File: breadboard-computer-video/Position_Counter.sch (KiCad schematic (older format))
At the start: 11 parts

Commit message: added things
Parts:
- removed U?: 74LS20, symbol 74xx:74LS20
- added U?: 74LS08, symbol 74xx:74LS08
- added U?: 74LS04, symbol 74xx:74LS04
- added U?: 74LS32, symbol 74xx:74LS32
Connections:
- wire segments 207 -> 209
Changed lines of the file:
@@
 Connection ~ 5650 2600
 Wire Wire Line
-	6650 2600 6650 5750
+	6650 2600 6650 3850
 Connection ~ 6650 2600
 Wire Wire Line
 	6650 2600 5650 2600
-Connection ~ 6650 5750
-Wire Wire Line
-	6650 5750 6950 5750
 NoConn ~ 3650 6200
 NoConn ~ 3450 6200
@@
 NoConn ~ 5350 6200
 Wire Wire Line
-	5550 6200 5550 6050
+	5550 6200 5550 6100
 Wire Wire Line
-	5550 6050 6100 6050
+	5550 6100 6100 6100
 Wire Wire Line
-	5250 6200 5250 5950
+	5250 6200 5250 6000
 Wire Wire Line
-	5250 5950 6100 5950
+	5250 6000 6100 6000
 Wire Wire Line
-	6700 6100 6800 6100
-Wire Wire Line
-	6800 6100 6800 7350
+	6700 6100 6750 6100
 Wire Wire Line
 	6800 7350 6250 7350
@@
 	1    0    0    -1
 $EndComp
-Wire Wire Line
-	4850 5750 6650 5750
 Connection ~ 4850 5750
 $Comp
-L 74xx:74LS20 U?
-U 2 1 5DE95783
+L 74xx:74LS08 U?
+U 1 1 5DED443E
 P 6400 6100
-F 0 "U?" H 6400 6475 50  0000 C CNN
-F 1 "74LS20" H 6400 6384 50  0000 C CNN
+F 0 "U?" H 6400 6425 50  0000 C CNN
+F 1 "74LS08" H 6400 6334 50  0000 C CNN
 F 2 "" H 6400 6100 50  0001 C CNN
-F 3 "http://www.ti.com/lit/gpn/sn74LS20" H 6400 6100 50  0001 C CNN
-	2    6400 6100
+F 3 "http://www.ti.com/lit/gpn/sn74LS08" H 6400 6100 50  0001 C CNN
+	1    6400 6100
 	1    0    0    -1
 $EndComp
 Wire Wire Line
-	6100 6150 6100 6250
+	6100 6100 6100 6200
+$Comp
+L 74xx:74LS04 U?
+U 1 1 5DF0C5CD
+P 6800 6400
+F 0 "U?" V 6754 6580 50  0000 L CNN
+F 1 "74LS04" V 6845 6580 50  0000 L CNN
+F 2 "" H 6800 6400 50  0001 C CNN
+F 3 "http://www.ti.com/lit/gpn/sn74LS04" H 6800 6400 50  0001 C CNN
+	1    6800 6400
+	0    1    1    0
+$EndComp
 Wire Wire Line
-	6100 6050 6100 6150
-Connection ~ 6100 6050
-Connection ~ 6100 6150
+	6800 6700 6800 7350
+$Comp
+L 74xx:74LS32 U?
+U 1 1 5DF1C351
+P 6650 4150
+F 0 "U?" V 6696 3970 50  0000 R CNN
+F 1 "74LS32" V 6605 3970 50  0000 R CNN
+F 2 "" H 6650 4150 50  0001 C CNN
+F 3 "http://www.ti.com/lit/gpn/sn74LS32" H 6650 4150 50  0001 C CNN
+	1    6650 4150
+	0    -1   -1   0
+$EndComp
+Wire Wire Line
+	4850 5750 6550 5750
+Wire Wire Line
+	6550 4450 6550 5750
+Connection ~ 6550 5750
+Wire Wire Line
+	6550 5750 6950 5750
+Wire Wire Line
+	6750 6100 6750 4450
+Connection ~ 6750 6100
+Wire Wire Line
+	6750 6100 6800 6100
 $EndSCHEMATC

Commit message: finished
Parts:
- removed U? (x5): 74LS161, symbol 74xx:74LS161
- added U?: 74LS04, symbol 74xx:74LS04
- added U? (x6): 74LS163, symbol 74xx:74LS163
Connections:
- net labels added: A0, A1, A2, A3, A4, A5, A6, A7, A8, A9, Earth, VBLANK, VCC
- wire segments 209 -> 230
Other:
- moved on the sheet: U?A

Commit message: fixed labels
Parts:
- removed U?: 74LS161, symbol 74xx:74LS161
- gave numbers to parts that had none: 13
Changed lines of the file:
@@
 CLK
 $Comp
-L 74xx:74LS83 U?
+L 74xx:74LS83 U28
 U 1 1 5DAF14DF
 P 2550 4150
-F 0 "U?" H 2550 5131 50  0000 C CNN
+F 0 "U28" H 2550 5131 50  0000 C CNN
 F 1 "74LS83" H 2550 5040 50  0000 C CNN
 F 2 "" H 2550 4150 50  0001 C CNN
@@
 $EndComp
 $Comp
-L 74xx:74LS83 U?
+L 74xx:74LS83 U32
 U 1 1 5DAF1910
 P 5650 4150
-F 0 "U?" H 5650 5131 50  0000 C CNN
+F 0 "U32" H 5650 5131 50  0000 C CNN
 F 1 "74LS83" H 5650 5040 50  0000 C CNN
 F 2 "" H 5650 4150 50  0001 C CNN
@@
 	7750 4650 8350 4650
 $Comp
-L 74xx:74LS83 U?
+L 74xx:74LS83 U37
 U 1 1 5DC079C4
 P 8850 4150
-F 0 "U?" H 8850 5131 50  0000 C CNN
+F 0 "U37" H 8850 5131 50  0000 C CNN
 F 1 "74LS83" H 8850 5040 50  0000 C CNN
 F 2 "" H 8850 4150 50  0001 C CNN
@@
 	6250 7250 6250 7100
 $Comp
-L 74xx:74LS20 U?
+L 74xx:74LS20 U30
 U 1 1 5DE7A035
 P 3750 5650
-F 0 "U?" H 3750 6025 50  0000 C CNN
+F 0 "U30" H 3750 6025 50  0000 C CNN
 F 1 "74LS20" H 3750 5934 50  0000 C CNN
 F 2 "" H 3750 5650 50  0001 C CNN
@@
 Connection ~ 4850 5650
 $Comp
-L 74xx:74LS08 U?
+L 74xx:74LS08 U34
 U 1 1 5DED443E
 P 6400 6000
-F 0 "U?" H 6400 6325 50  0000 C CNN
+F 0 "U34" H 6400 6325 50  0000 C CNN
 F 1 "74LS08" H 6400 6234 50  0000 C CNN
 F 2 "" H 6400 6000 50  0001 C CNN
@@
 	6100 6000 6100 6100
 $Comp
-L 74xx:74LS04 U?
+L 74xx:74LS04 U19
 U 1 1 5DF0C5CD
 P 6800 6300
-F 0 "U?" V 6754 6480 50  0000 L CNN
+F 0 "U19" V 6754 6480 50  0000 L CNN
 F 1 "74LS04" V 6845 6480 50  0000 L CNN
 F 2 "" H 6800 6300 50  0001 C CNN
@@
 	6800 6600 6800 7250
 $Comp
-L 74xx:74LS32 U?
+L 74xx:74LS32 U35
 U 1 1 5DF1C351
 P 6650 4150
-F 0 "U?" V 6696 3970 50  0000 R CNN
+F 0 "U35" V 6696 3970 50  0000 R CNN
 F 1 "74LS32" V 6605 3970 50  0000 R CNN
 F 2 "" H 6650 4150 50  0001 C CNN
@@
 	6150 2500 9350 2500
 $Comp
-L 74xx:74LS04 U?
+L 74xx:74LS04 U19
 U 2 1 5E085A92
 P 1250 1700
-F 0 "U?" V 1204 1880 50  0000 L CNN
+F 0 "U19" V 1204 1880 50  0000 L CNN
 F 1 "74LS04" V 1295 1880 50  0000 L CNN
 F 2 "" H 1250 1700 50  0001 C CNN
@@
 A9
 $Comp
-L 74xx:74LS163 U?
+L 74xx:74LS163 U27
 U 1 1 5E0C0473
 P 2550 1900
-F 0 "U?" V 2596 1056 50  0000 R CNN
+F 0 "U27" V 2596 1056 50  0000 R CNN
 F 1 "74LS163" V 2505 1056 50  0000 R CNN
 F 2 "" H 2550 1900 50  0001 C CNN
@@
 $EndComp
 $Comp
-L 74xx:74LS163 U?
+L 74xx:74LS163 U31
 U 1 1 5E0F4790
 P 5650 1900
-F 0 "U?" V 5696 1056 50  0000 R CNN
+F 0 "U31" V 5696 1056 50  0000 R CNN
 F 1 "74LS163" V 5605 1056 50  0000 R CNN
 F 2 "" H 5650 1900 50  0001 C CNN
@@
 $EndComp
 $Comp
-L 74xx:74LS163 U?
+L 74xx:74LS163 U36
 U 1 1 5E1044B1
 P 8850 1900
-F 0 "U?" V 8896 1056 50  0000 R CNN
+F 0 "U36" V 8896 1056 50  0000 R CNN
 F 1 "74LS163" V 8805 1056 50  0000 R CNN
 F 2 "" H 8850 1900 50  0001 C CNN
@@
 $EndComp
 $Comp
-L 74xx:74LS163 U?
+L 74xx:74LS163 U26
 U 1 1 5E115C5E
 P 1550 6600
-F 0 "U?" V 1596 5756 50  0000 R CNN
+F 0 "U26" V 1596 5756 50  0000 R CNN
 F 1 "74LS163" V 1505 5756 50  0000 R CNN
 F 2 "" H 1550 6600 50  0001 C CNN
@@
 $EndComp
 $Comp
-L 74xx:74LS163 U?
+L 74xx:74LS163 U29
 U 1 1 5E125B51
 P 3650 6600
-F 0 "U?" V 3696 5756 50  0000 R CNN
+F 0 "U29" V 3696 5756 50  0000 R CNN
 F 1 "74LS163" V 3605 5756 50  0000 R CNN
 F 2 "" H 3650 6600 50  0001 C CNN
@@
 $EndComp
 $Comp
-L 74xx:74LS163 U?
+L 74xx:74LS163 U33
 U 1 1 5E1357C5
 P 5750 6600
-F 0 "U?" V 5796 5756 50  0000 R CNN
+F 0 "U33" V 5796 5756 50  0000 R CNN
 F 1 "74LS163" V 5705 5756 50  0000 R CNN
 F 2 "" H 5750 6600 50  0001 C CNN
@@
 	0    -1   -1   0
 $EndComp
-$Comp
-L 74xx:74LS161 U?
-U 1 1 5DAF4BC7
-P 1550 6600
-F 0 "U?" V 1596 5756 50  0000 R CNN
-F 1 "74LS161" V 1505 5756 50  0000 R CNN
-F 2 "" H 1550 6600 50  0001 C CNN
-F 3 "http://www.ti.com/lit/gpn/sn74LS161" H 1550 6600 50  0001 C CNN
-	1    1550 6600
-	0    -1   -1   0
-$EndComp

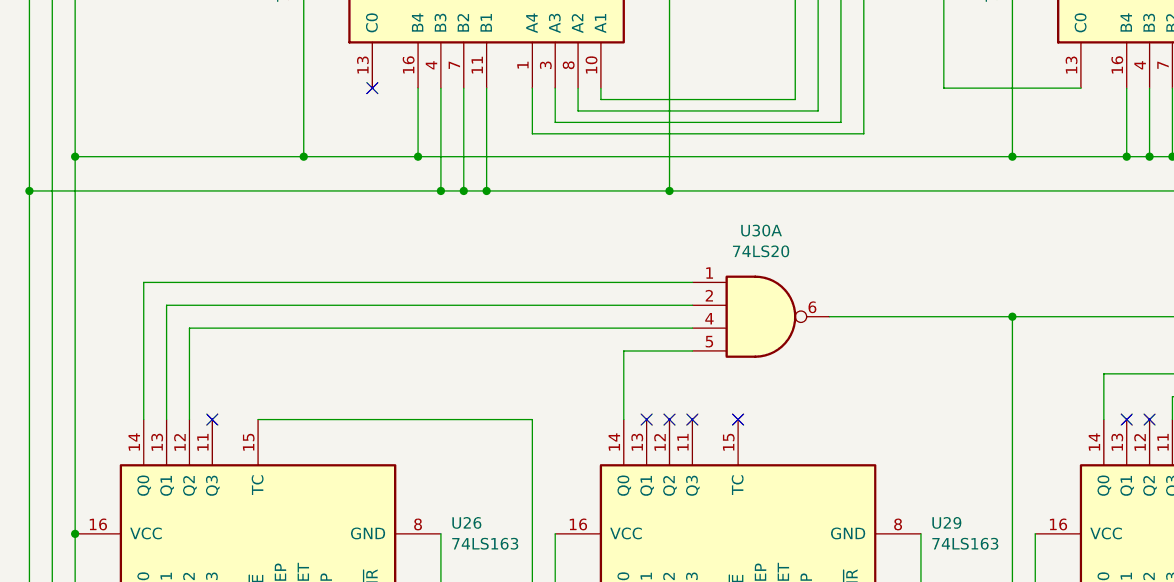
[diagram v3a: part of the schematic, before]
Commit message: Change 74LS20 to 74LS30
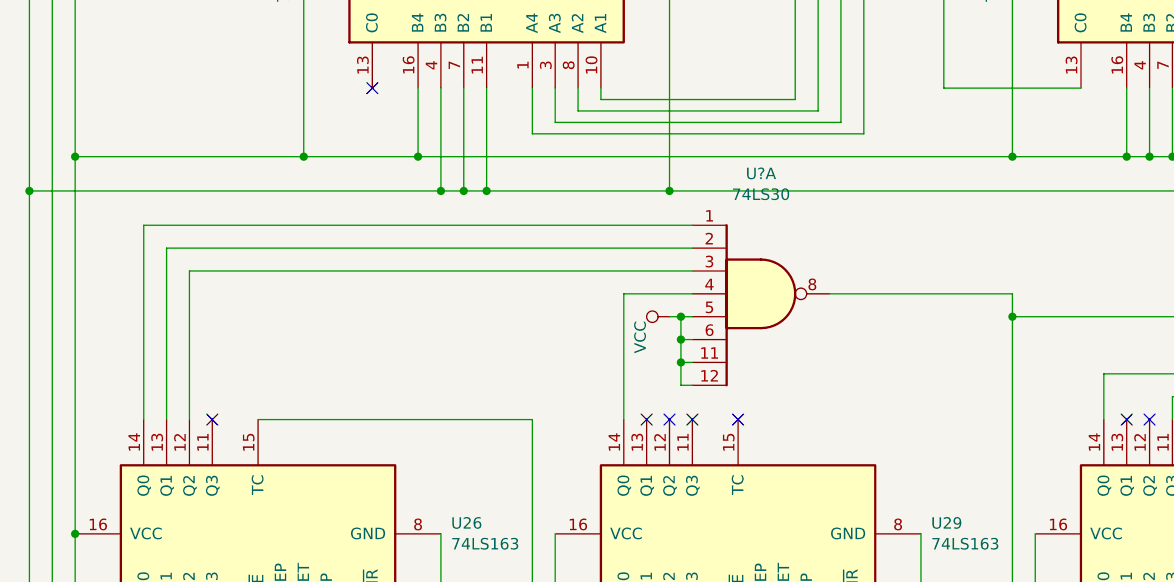
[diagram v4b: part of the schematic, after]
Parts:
- removed U30: 74LS20, symbol 74xx:74LS20
- added U?: 74LS30, symbol 74xx:74LS30
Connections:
- net VCC: now also U?.11, U?.12, U?.5, U?.6
- net at U26.14 (Q0): now also U?.1
- net at U26.13 (Q1): now also U?.2
- net at U26.12 (Q2): now also U?.3
- net at U29.14 (Q0): now also U?.4
- net at U26.1 (~MR), U29.1 (~MR), U33.2 (CP)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: now also U?.8
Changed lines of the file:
@@
 Wire Wire Line
 	2450 4650 2450 5100
-Wire Wire Line
-	2550 4650 2550 5100
 Connection ~ 2550 5100
 Wire Wire Line
@@
 	4950 7500 5750 7500
 Wire Wire Line
-	3450 5800 3150 5800
-Wire Wire Line
-	3150 5800 3150 6100
-Wire Wire Line
-	3450 5700 1250 5700
-Wire Wire Line
-	1250 5700 1250 6100
-Wire Wire Line
-	3450 5600 1150 5600
-Wire Wire Line
-	1150 5600 1150 6100
-Wire Wire Line
-	3450 5500 1050 5500
-Wire Wire Line
-	1050 5500 1050 6100
-Wire Wire Line
-	4050 5650 4850 5650
+	3450 5550 3150 5550
+Wire Wire Line
+	3150 5550 3150 6100
+Wire Wire Line
+	3450 5450 1250 5450
+Wire Wire Line
+	1250 5450 1250 6100
+Wire Wire Line
+	3450 5350 1150 5350
+Wire Wire Line
+	1150 5350 1150 6100
+Wire Wire Line
+	3450 5250 1050 5250
+Wire Wire Line
+	1050 5250 1050 6100
 Wire Wire Line
 	6050 7400 6050 7100
@@
 Wire Wire Line
 	6250 7250 6250 7100
-$Comp
-L 74xx:74LS20 U30
-U 1 1 5DE7A035
-P 3750 5650
-F 0 "U30" H 3750 6025 50  0000 C CNN
-F 1 "74LS20" H 3750 5934 50  0000 C CNN
-F 2 "" H 3750 5650 50  0001 C CNN
-F 3 "http://www.ti.com/lit/gpn/sn74LS20" H 3750 5650 50  0001 C CNN
-	1    3750 5650
-	1    0    0    -1
-$EndComp
 Connection ~ 4850 5650
 $Comp
@@
 	0    -1   -1   0
 $EndComp
+$Comp
+L 74xx:74LS30 U?
+U 1 1 5DB99F71
+P 3750 5550
+F 0 "U?" H 3750 6075 50  0000 C CNN
+F 1 "74LS30" H 3750 5984 50  0000 C CNN
+F 2 "" H 3750 5550 50  0001 C CNN
+F 3 "http://www.ti.com/lit/gpn/sn74LS30" H 3750 5550 50  0001 C CNN
+	1    3750 5550
+	1    0    0    -1
+$EndComp
+Wire Wire Line
+	2550 4650 2550 5100
+Wire Wire Line
+	4850 5550 4850 5650
+Wire Wire Line
+	4050 5550 4850 5550
+$Comp
+L power:VCC #PWR?
+U 1 1 5DC2EC08
+P 3350 5650
+F 0 "#PWR?" H 3350 5500 50  0001 C CNN
+F 1 "VCC" H 3368 5777 50  0000 L CNN
+F 2 "" H 3350 5650 50  0001 C CNN
+F 3 "" H 3350 5650 50  0001 C CNN
+	1    3350 5650
+	0    -1   1    0
+$EndComp
+Wire Wire Line
+	3400 5650 3400 5750
+Wire Wire Line
+	3400 5750 3450 5750
+Connection ~ 3400 5650
+Wire Wire Line
+	3400 5650 3450 5650
+Wire Wire Line
+	3350 5650 3400 5650
+Wire Wire Line
+	3400 5750 3400 5850
+Wire Wire Line
+	3400 5850 3450 5850
+Connection ~ 3400 5750
+Wire Wire Line
+	3400 5850 3400 5950
+Wire Wire Line
+	3400 5950 3450 5950
+Connection ~ 3400 5850
 $EndSCHEMATC

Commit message: added vram data register
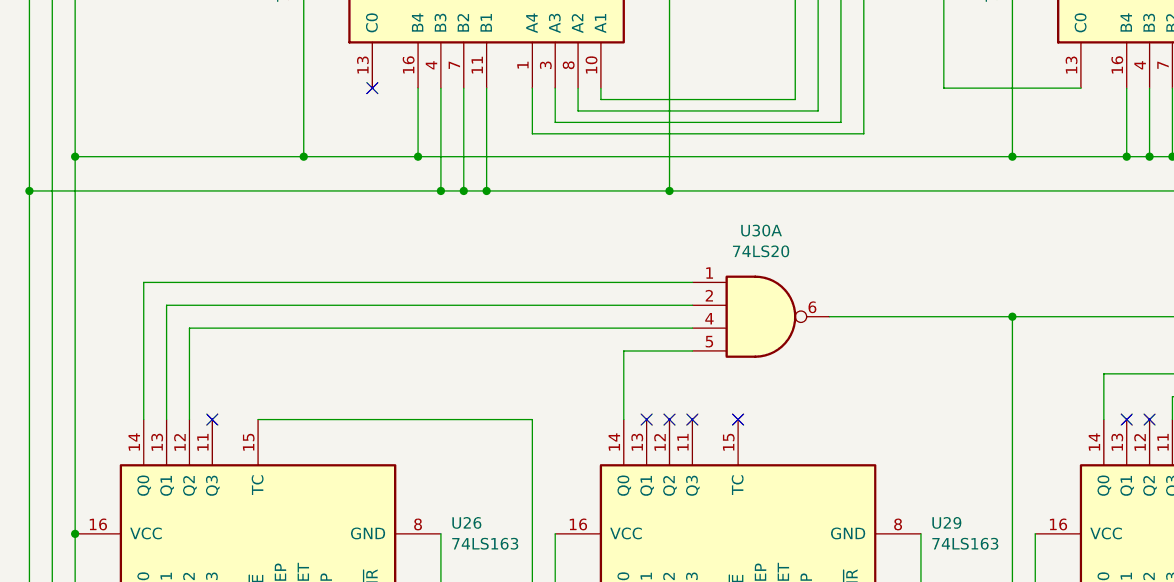
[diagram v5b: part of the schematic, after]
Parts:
- removed U?: 74LS30, symbol 74xx:74LS30
- added U30: 74LS20, symbol 74xx:74LS20
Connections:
- net at U26.14 (Q0): now also U30.1
- net at U26.13 (Q1): now also U30.2
- net at U26.12 (Q2): now also U30.4
- net at U29.14 (Q0): now also U30.5
- net at U26.1 (~MR), U29.1 (~MR), U33.2 (CP)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: now also U30.6
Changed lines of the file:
@@
 Wire Wire Line
 	2450 4650 2450 5100
+Wire Wire Line
+	2550 4650 2550 5100
 Connection ~ 2550 5100
 Wire Wire Line
@@
 	4950 7500 5750 7500
 Wire Wire Line
-	3450 5550 3150 5550
-Wire Wire Line
-	3150 5550 3150 6100
-Wire Wire Line
-	3450 5450 1250 5450
-Wire Wire Line
-	1250 5450 1250 6100
-Wire Wire Line
-	3450 5350 1150 5350
-Wire Wire Line
-	1150 5350 1150 6100
-Wire Wire Line
-	3450 5250 1050 5250
-Wire Wire Line
-	1050 5250 1050 6100
+	3450 5800 3150 5800
+Wire Wire Line
+	3150 5800 3150 6100
+Wire Wire Line
+	3450 5700 1250 5700
+Wire Wire Line
+	1250 5700 1250 6100
+Wire Wire Line
+	3450 5600 1150 5600
+Wire Wire Line
+	1150 5600 1150 6100
+Wire Wire Line
+	3450 5500 1050 5500
+Wire Wire Line
+	1050 5500 1050 6100
+Wire Wire Line
+	4050 5650 4850 5650
 Wire Wire Line
 	6050 7400 6050 7100
@@
 Wire Wire Line
 	6250 7250 6250 7100
+$Comp
+L 74xx:74LS20 U30
+U 1 1 5DE7A035
+P 3750 5650
+F 0 "U30" H 3750 6025 50  0000 C CNN
+F 1 "74LS20" H 3750 5934 50  0000 C CNN
+F 2 "" H 3750 5650 50  0001 C CNN
+F 3 "http://www.ti.com/lit/gpn/sn74LS20" H 3750 5650 50  0001 C CNN
+	1    3750 5650
+	1    0    0    -1
+$EndComp
 Connection ~ 4850 5650
 $Comp
@@
 	0    -1   -1   0
 $EndComp
-$Comp
-L 74xx:74LS30 U?
-U 1 1 5DB99F71
-P 3750 5550
-F 0 "U?" H 3750 6075 50  0000 C CNN
-F 1 "74LS30" H 3750 5984 50  0000 C CNN
-F 2 "" H 3750 5550 50  0001 C CNN
-F 3 "http://www.ti.com/lit/gpn/sn74LS30" H 3750 5550 50  0001 C CNN
-	1    3750 5550
-	1    0    0    -1
-$EndComp
-Wire Wire Line
-	2550 4650 2550 5100
-Wire Wire Line
-	4850 5550 4850 5650
-Wire Wire Line
-	4050 5550 4850 5550
-$Comp
-L power:VCC #PWR?
-U 1 1 5DC2EC08
-P 3350 5650
-F 0 "#PWR?" H 3350 5500 50  0001 C CNN
-F 1 "VCC" H 3368 5777 50  0000 L CNN
-F 2 "" H 3350 5650 50  0001 C CNN
-F 3 "" H 3350 5650 50  0001 C CNN
-	1    3350 5650
-	0    -1   1    0
-$EndComp
-Wire Wire Line
-	3400 5650 3400 5750
-Wire Wire Line
-	3400 5750 3450 5750
-Connection ~ 3400 5650
-Wire Wire Line
-	3400 5650 3450 5650
-Wire Wire Line
-	3350 5650 3400 5650
-Wire Wire Line
-	3400 5750 3400 5850
-Wire Wire Line
-	3400 5850 3450 5850
-Connection ~ 3400 5750
-Wire Wire Line
-	3400 5850 3400 5950
-Wire Wire Line
-	3400 5950 3450 5950
-Connection ~ 3400 5850
 $EndSCHEMATC

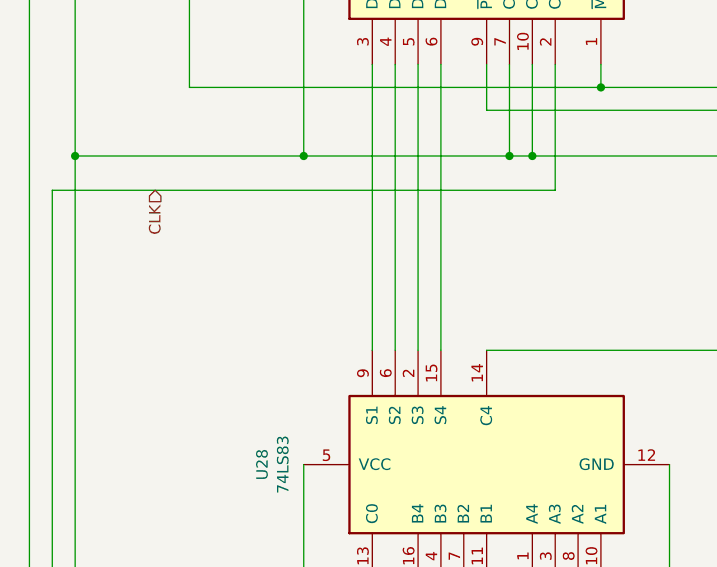
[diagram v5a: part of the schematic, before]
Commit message: Eliminated a redundant 74ls163, which was only necessary when the character cells were not of equal width and height
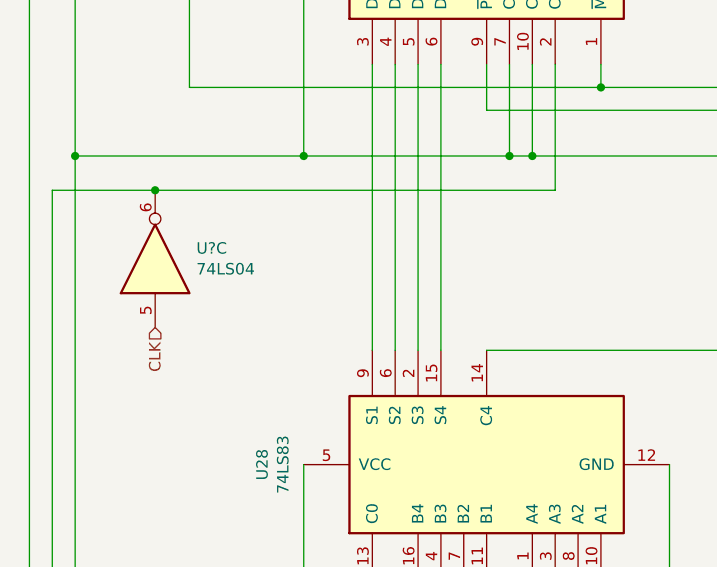
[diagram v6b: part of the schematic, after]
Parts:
- added U?: 74LS04, symbol 74xx:74LS04
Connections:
- net CLK: now also U?.5; no longer U26.2 (CP), U27.2 (CP)
- new net: U26.2 (CP), U27.2 (CP), U?.6
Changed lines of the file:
@@
 Comment4 ""
 $EndDescr
-Text HLabel 1100 2950 3    50   Input ~ 0
+Text HLabel 1100 3550 3    50   Input ~ 0
 CLK
 $Comp
@@
 Connection ~ 550  5100
 Wire Wire Line
-	650  2950 2850 2950
+	650  2950 1100 2950
 Wire Wire Line
 	650  2950 650  7300
@@
 	0    -1   -1   0
 $EndComp
+$Comp
+L 74xx:74LS04 U?
+U 3 1 5E00B3C7
+P 1100 3250
+F 0 "U?" V 1146 3070 50  0000 R CNN
+F 1 "74LS04" V 1055 3070 50  0000 R CNN
+F 2 "" H 1100 3250 50  0001 C CNN
+F 3 "http://www.ti.com/lit/gpn/sn74LS04" H 1100 3250 50  0001 C CNN
+	3    1100 3250
+	0    -1   -1   0
+$EndComp
+Connection ~ 1100 2950
+Wire Wire Line
+	1100 2950 2850 2950
 $EndSCHEMATC

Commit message: finished hv sync
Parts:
- gave numbers to parts that had none: 1
- renumbered U19 to U22, U27 to U23, U31 to U24, U36 to U25, U28 to U27, U32 to U28, U35 to U29, U37 to U30, U30 to U31, U34 to U32, U26 to U33, U29 to U34, U33 to U35
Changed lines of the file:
@@
 CLK
 $Comp
-L 74xx:74LS83 U28
+L 74xx:74LS83 U27
 U 1 1 5DAF14DF
 P 2550 4150
-F 0 "U28" H 2550 5131 50  0000 C CNN
+F 0 "U27" H 2550 5131 50  0000 C CNN
 F 1 "74LS83" H 2550 5040 50  0000 C CNN
 F 2 "" H 2550 4150 50  0001 C CNN
@@
 $EndComp
 $Comp
-L 74xx:74LS83 U32
+L 74xx:74LS83 U28
 U 1 1 5DAF1910
 P 5650 4150
-F 0 "U32" H 5650 5131 50  0000 C CNN
+F 0 "U28" H 5650 5131 50  0000 C CNN
 F 1 "74LS83" H 5650 5040 50  0000 C CNN
 F 2 "" H 5650 4150 50  0001 C CNN
@@
 	7750 4650 8350 4650
 $Comp
-L 74xx:74LS83 U37
+L 74xx:74LS83 U30
 U 1 1 5DC079C4
 P 8850 4150
-F 0 "U37" H 8850 5131 50  0000 C CNN
+F 0 "U30" H 8850 5131 50  0000 C CNN
 F 1 "74LS83" H 8850 5040 50  0000 C CNN
 F 2 "" H 8850 4150 50  0001 C CNN
@@
 	6250 7250 6250 7100
 $Comp
-L 74xx:74LS20 U30
+L 74xx:74LS20 U31
 U 1 1 5DE7A035
 P 3750 5650
-F 0 "U30" H 3750 6025 50  0000 C CNN
+F 0 "U31" H 3750 6025 50  0000 C CNN
 F 1 "74LS20" H 3750 5934 50  0000 C CNN
 F 2 "" H 3750 5650 50  0001 C CNN
@@
 Connection ~ 4850 5650
 $Comp
-L 74xx:74LS08 U34
+L 74xx:74LS08 U32
 U 1 1 5DED443E
 P 6400 6000
-F 0 "U34" H 6400 6325 50  0000 C CNN
+F 0 "U32" H 6400 6325 50  0000 C CNN
 F 1 "74LS08" H 6400 6234 50  0000 C CNN
 F 2 "" H 6400 6000 50  0001 C CNN
@@
 	6100 6000 6100 6100
 $Comp
-L 74xx:74LS04 U19
+L 74xx:74LS04 U22
 U 1 1 5DF0C5CD
 P 6800 6300
-F 0 "U19" V 6754 6480 50  0000 L CNN
+F 0 "U22" V 6754 6480 50  0000 L CNN
 F 1 "74LS04" V 6845 6480 50  0000 L CNN
 F 2 "" H 6800 6300 50  0001 C CNN
@@
 	6800 6600 6800 7250
 $Comp
-L 74xx:74LS32 U35
+L 74xx:74LS32 U29
 U 1 1 5DF1C351
 P 6650 4150
-F 0 "U35" V 6696 3970 50  0000 R CNN
+F 0 "U29" V 6696 3970 50  0000 R CNN
 F 1 "74LS32" V 6605 3970 50  0000 R CNN
 F 2 "" H 6650 4150 50  0001 C CNN
@@
 	6150 2500 9350 2500
 $Comp
-L 74xx:74LS04 U19
+L 74xx:74LS04 U22
 U 2 1 5E085A92
 P 1250 1700
-F 0 "U19" V 1204 1880 50  0000 L CNN
+F 0 "U22" V 1204 1880 50  0000 L CNN
 F 1 "74LS04" V 1295 1880 50  0000 L CNN
 F 2 "" H 1250 1700 50  0001 C CNN
@@
 A9
 $Comp
-L 74xx:74LS163 U27
+L 74xx:74LS163 U23
 U 1 1 5E0C0473
 P 2550 1900
-F 0 "U27" V 2596 1056 50  0000 R CNN
+F 0 "U23" V 2596 1056 50  0000 R CNN
 F 1 "74LS163" V 2505 1056 50  0000 R CNN
 F 2 "" H 2550 1900 50  0001 C CNN
@@
 $EndComp
 $Comp
-L 74xx:74LS163 U31
+L 74xx:74LS163 U24
 U 1 1 5E0F4790
 P 5650 1900
-F 0 "U31" V 5696 1056 50  0000 R CNN
+F 0 "U24" V 5696 1056 50  0000 R CNN
 F 1 "74LS163" V 5605 1056 50  0000 R CNN
 F 2 "" H 5650 1900 50  0001 C CNN
@@
 $EndComp
 $Comp
-L 74xx:74LS163 U36
+L 74xx:74LS163 U25
 U 1 1 5E1044B1
 P 8850 1900
-F 0 "U36" V 8896 1056 50  0000 R CNN
+F 0 "U25" V 8896 1056 50  0000 R CNN
 F 1 "74LS163" V 8805 1056 50  0000 R CNN
 F 2 "" H 8850 1900 50  0001 C CNN
@@
 $EndComp
 $Comp
-L 74xx:74LS163 U26
+L 74xx:74LS163 U33
 U 1 1 5E115C5E
 P 1550 6600
-F 0 "U26" V 1596 5756 50  0000 R CNN
+F 0 "U33" V 1596 5756 50  0000 R CNN
 F 1 "74LS163" V 1505 5756 50  0000 R CNN
 F 2 "" H 1550 6600 50  0001 C CNN
@@
 $EndComp
 $Comp
-L 74xx:74LS163 U29
+L 74xx:74LS163 U34
 U 1 1 5E125B51
 P 3650 6600
-F 0 "U29" V 3696 5756 50  0000 R CNN
+F 0 "U34" V 3696 5756 50  0000 R CNN
 F 1 "74LS163" V 3605 5756 50  0000 R CNN
 F 2 "" H 3650 6600 50  0001 C CNN
@@
 $EndComp
 $Comp
-L 74xx:74LS163 U33
+L 74xx:74LS163 U35
 U 1 1 5E1357C5
 P 5750 6600
-F 0 "U33" V 5796 5756 50  0000 R CNN
+F 0 "U35" V 5796 5756 50  0000 R CNN
 F 1 "74LS163" V 5705 5756 50  0000 R CNN
 F 2 "" H 5750 6600 50  0001 C CNN
@@
 $EndComp
 $Comp
-L 74xx:74LS04 U?
+L 74xx:74LS04 U26
 U 3 1 5E00B3C7
 P 1100 3250
-F 0 "U?" V 1146 3070 50  0000 R CNN
+F 0 "U26" V 1146 3070 50  0000 R CNN
 F 1 "74LS04" V 1055 3070 50  0000 R CNN
 F 2 "" H 1100 3250 50  0001 C CNN
